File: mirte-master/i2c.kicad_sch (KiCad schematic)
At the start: 0 parts

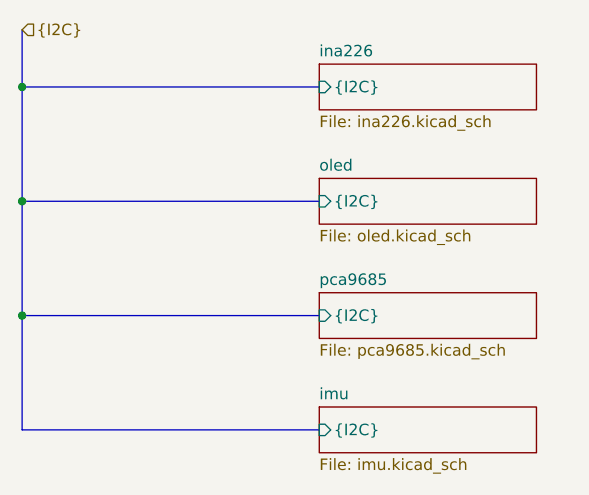
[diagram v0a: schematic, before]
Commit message: mirte-master schematic cleanup and readabilityimprovements
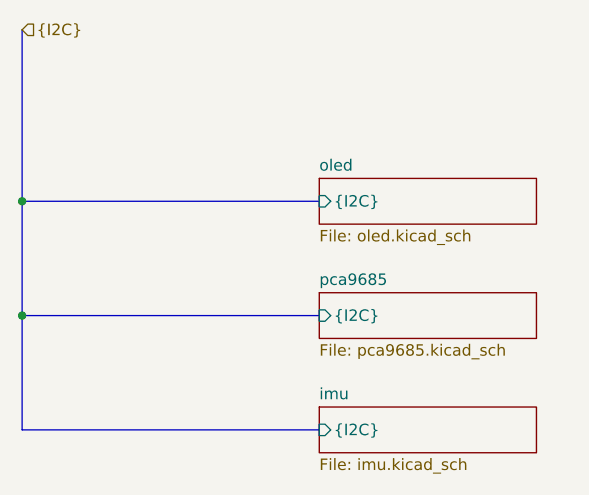
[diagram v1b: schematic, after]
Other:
- removed sheet ina226
- title: (none) -> ${PROJECTNAME}
